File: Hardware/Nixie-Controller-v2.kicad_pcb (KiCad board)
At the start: 4 copper layers, 220 x 65 mm, 216 parts, among them J7 12V DC JACK, U1 MAX1771, U10 74HC4067, U11 M41T01, U12 STM32F103C8, U13 OPA180, U14 74HC4067, U15 OPA180, U16 74HC4067, U17 OPA180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

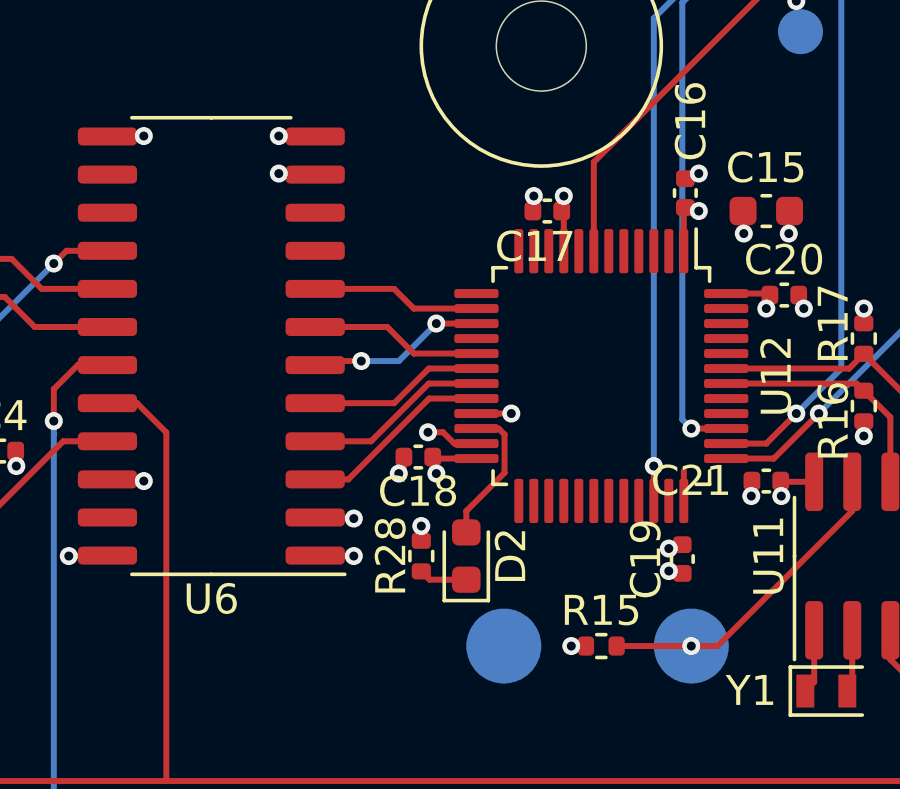
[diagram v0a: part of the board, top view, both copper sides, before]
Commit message: Connect shift register to SPI ports
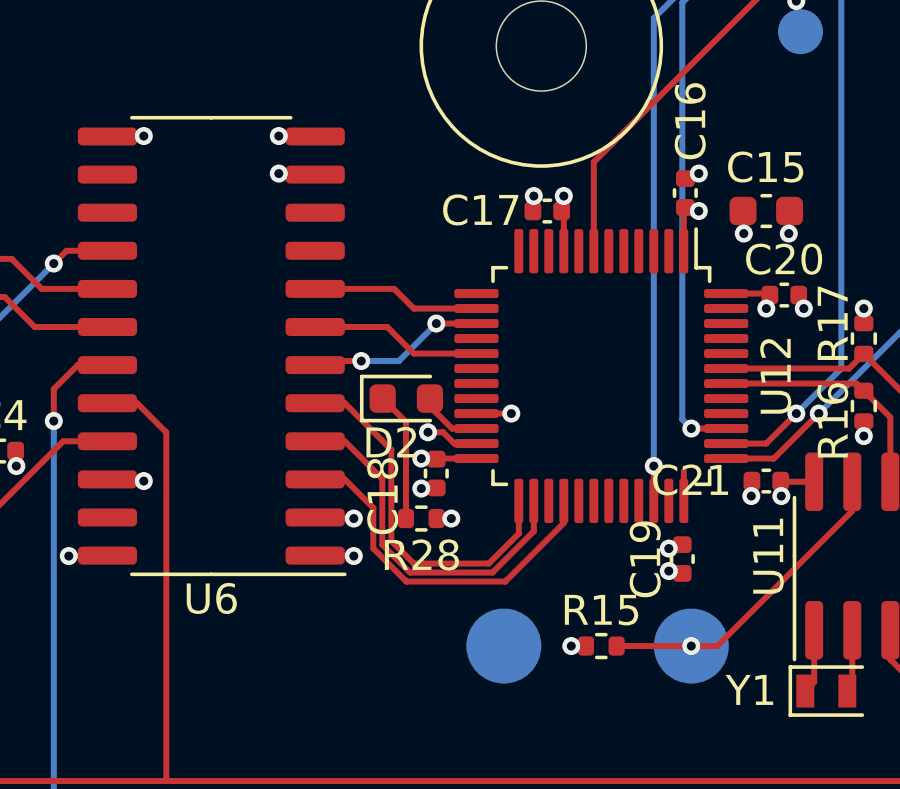
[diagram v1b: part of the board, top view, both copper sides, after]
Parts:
- moved D2 5.62 mm to (119.5, 74.8), turned to 0 degrees
- moved R28 1.25 mm to (120.0, 78.8), turned to 180 degrees
- moved C18 0.81 mm to (120.5, 77.2), turned to 270 degrees
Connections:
- U12 pad 18: 3V3_SR_LATCH -> Net-(U12-Pad18)
- U12 pad 19: 3V3_SR_SHIFT -> Net-(U12-Pad19)
- U12 pad 20: 3V3_SR_DATA -> Net-(U12-Pad20)
- U12 pad 25: Net-(U12-Pad25) -> 3V3_SR_nCS
- U12 pad 26: Net-(U12-Pad26) -> 3V3_SR_SCK
- U12 pad 28: Net-(U12-Pad28) -> 3V3_SR_MOSI
- U6 pad 3: 3V3_SR_DATA -> 3V3_SR_MOSI
- U6 pad 4: 3V3_SR_SHIFT -> 3V3_SR_SCK
- U6 pad 5: 3V3_SR_LATCH -> 3V3_SR_nCS
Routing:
- net 3V3_SR_nCS: track 0.00 -> 12.3 mm
- net 3V3_SR_MOSI: track 0.00 -> 12.0 mm
- net 3V3_SR_SCK: track 0.00 -> 12.0 mm
- net 3V3_SR_DATA: track 6.49 -> 0.00 mm
- net 3V3_SR_SHIFT: track 6.17 -> 0.00 mm
- net 3V3_SR_LATCH: track 5.85 -> 0.00 mm
- net Net-(D2-Pad1): track 1.61 -> 4.32 mm
- net Net-(D2-Pad2): track 4.81 -> 2.12 mm

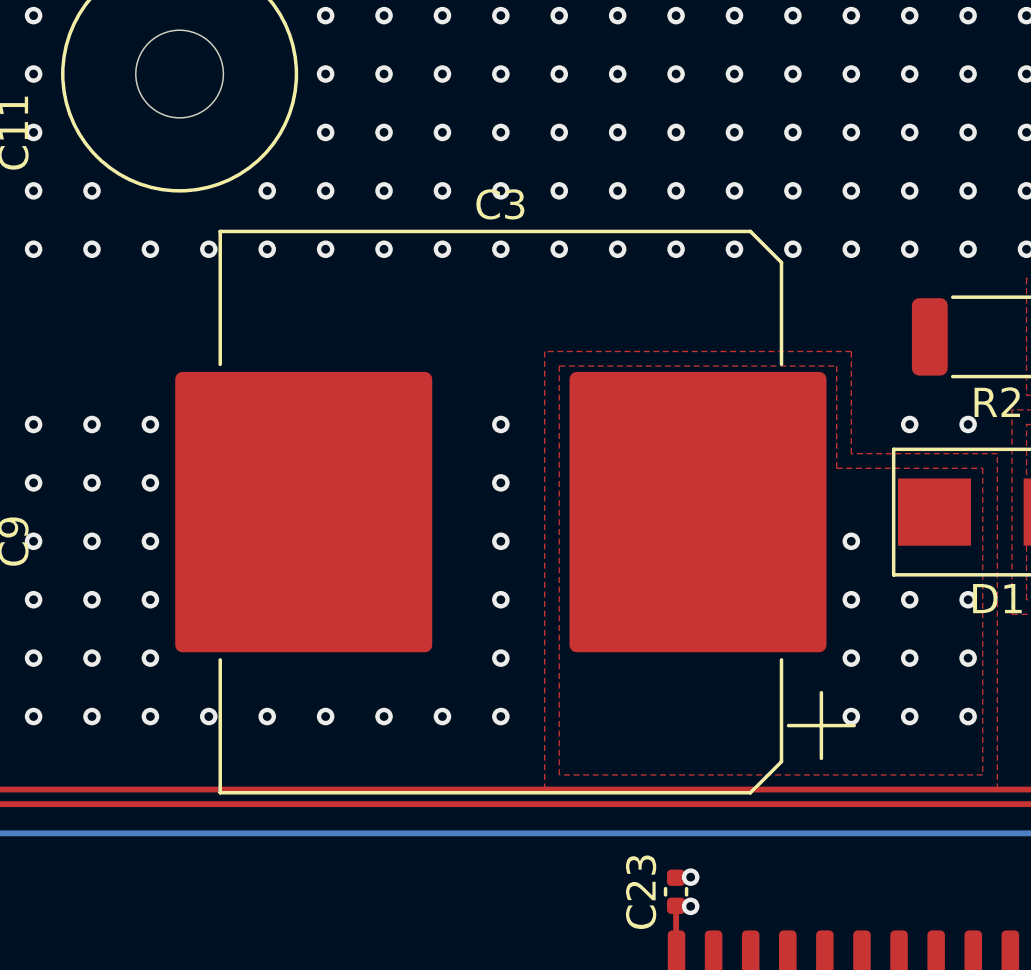
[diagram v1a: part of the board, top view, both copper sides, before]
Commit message: Switch HV output cap to 10uF
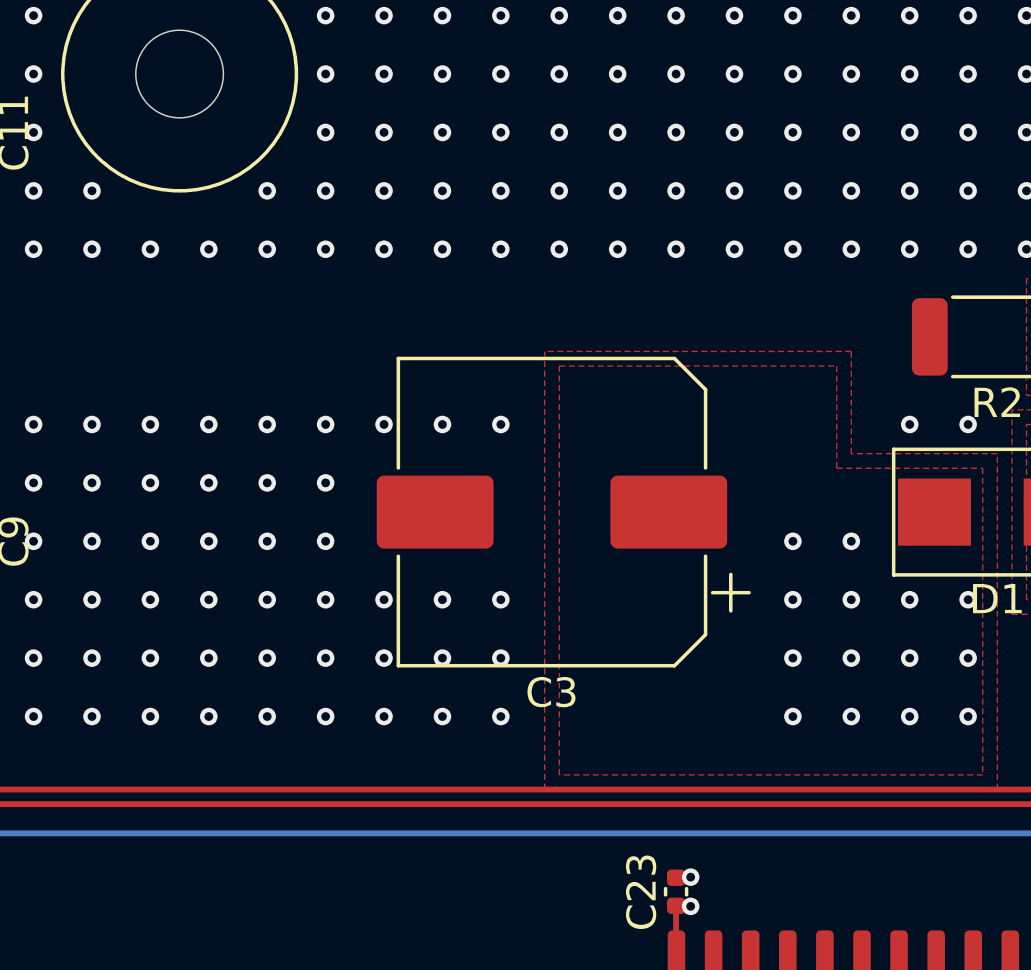
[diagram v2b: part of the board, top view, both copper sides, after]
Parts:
- C3: value 22uF -> 10uF; footprint Capacitor_SMD:CP_Elec_18x17.5 -> Capacitor_SMD:CP_Elec_10x10
- moved C3 1.75 mm to (206.8, 78.0)
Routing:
- net GND: vias 413 -> 432
- net +HV: vias 11 -> 15

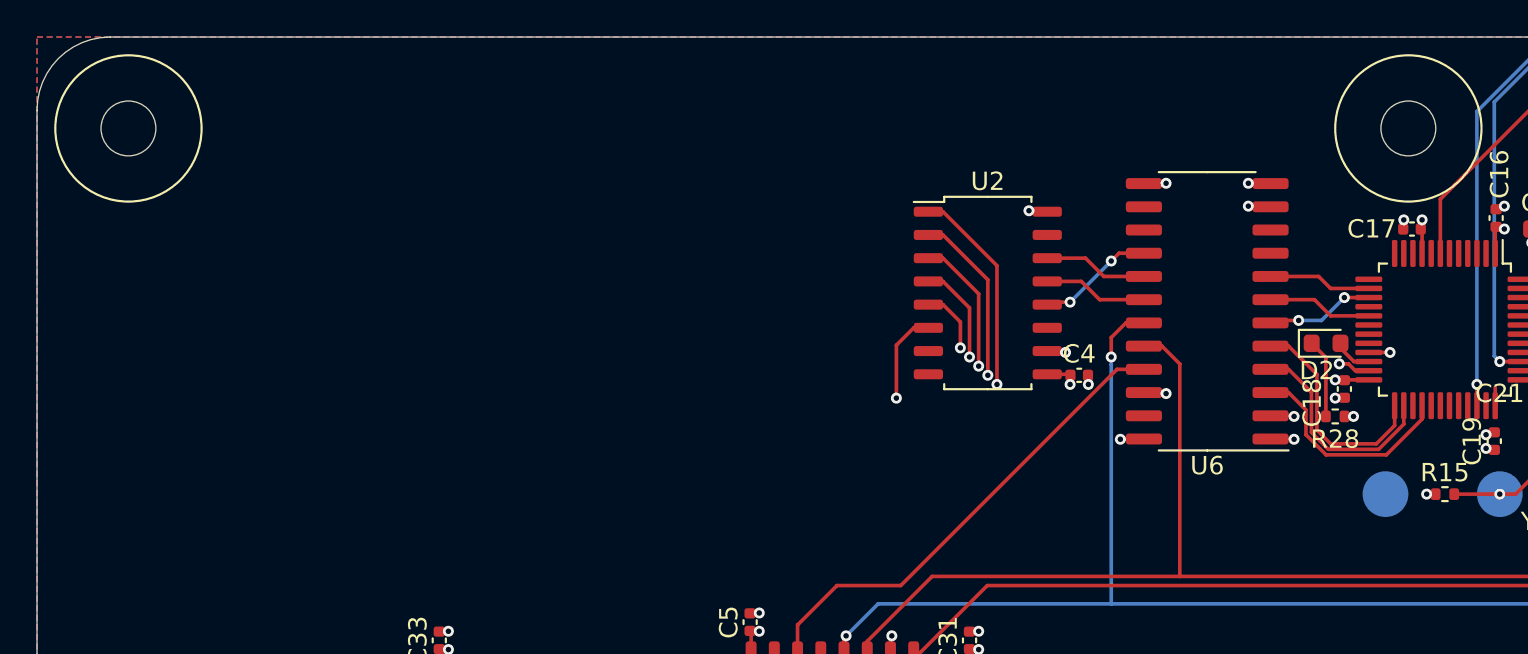
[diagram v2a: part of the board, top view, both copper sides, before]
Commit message: Add ESP WiFi module
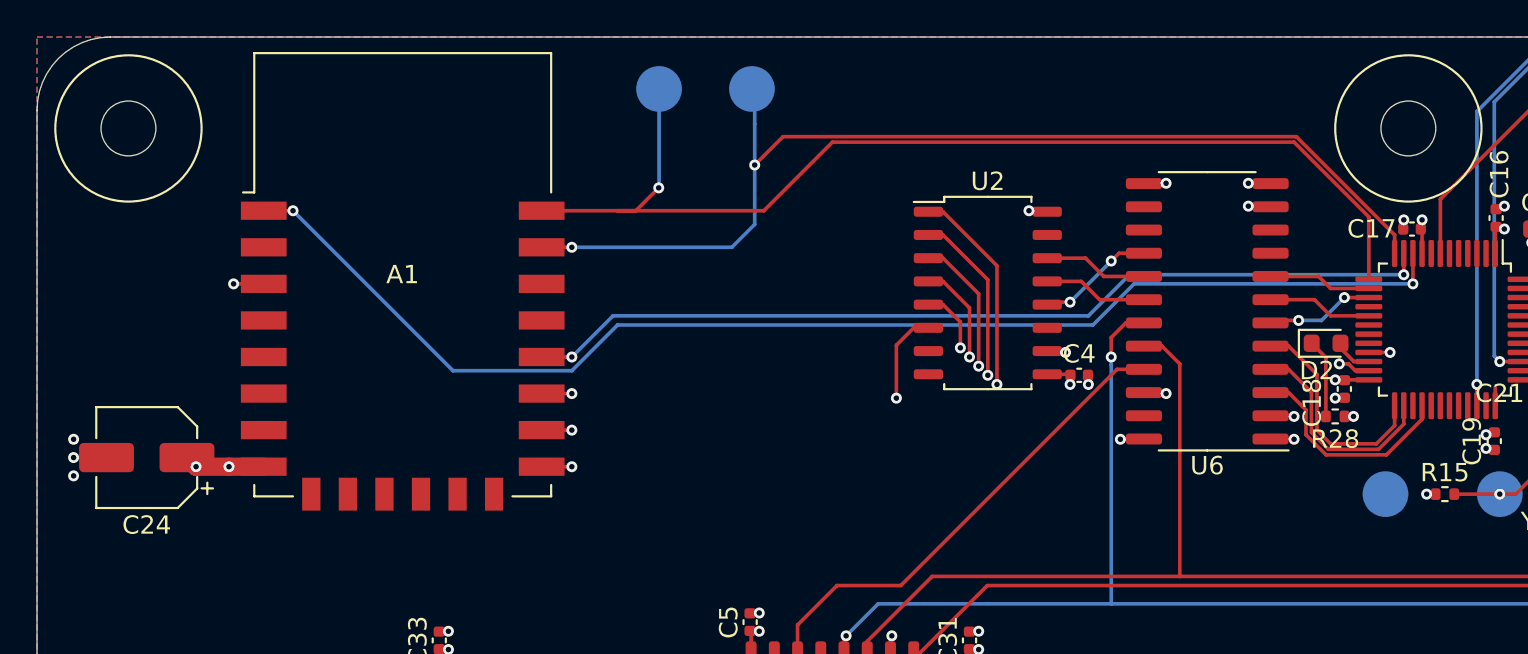
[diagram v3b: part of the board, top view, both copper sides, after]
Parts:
- added A1: ESP-12F, RF_Module:ESP-12E, F.Cu at (69.0, 71.0)
- added C24: 47uF, Capacitor_SMD:CP_Elec_5x5.3, F.Cu at (55.0, 81.0)
- added TP17: TX, TestPoint:TestPoint_Pad_D2.5mm, B.Cu at (83.0, 60.8)
- added TP18: RX, TestPoint:TestPoint_Pad_D2.5mm, B.Cu at (88.1, 60.8)
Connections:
- U12 pad 10: Net-(U12-Pad10) -> ESP_nRST
- U12 pad 11: Net-(U12-Pad11) -> ESP_RUN
- U12 pad 12: Net-(U12-Pad12) -> ESP_TX
- U12 pad 13: Net-(U12-Pad13) -> ESP_RX
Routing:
- net ESP_nRST: track 0.00 -> 70.1 mm, vias 0 -> 2
- net ESP_RX: track 0.00 -> 60.1 mm, vias 0 -> 1
- net ESP_TX: track 0.00 -> 58.5 mm, vias 0 -> 2
- net ESP_RUN: track 0.00 -> 50.2 mm, vias 0 -> 2
- net +3V3: track 23.7 -> 31.4 mm, vias 29 -> 33
- net GND: track 68.8 -> 72.1 mm, vias 432 -> 437
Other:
- board text added: "RX"
- board text added: "TX"

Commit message: Add author and HV info to silkscreen
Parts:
- added REF**: Symbol_Highvoltage_Type1_CopperTop_Small, Symbol:Symbol_Highvoltage_Type1_CopperTop_Small, B.Cu at (87.0, 114.0)
- added REF**: Symbol_Highvoltage_Type1_CopperTop_Small, Symbol:Symbol_Highvoltage_Type1_CopperTop_Small, B.Cu at (116.0, 114.0)
- added REF**: Symbol_Highvoltage_Type1_CopperTop_Small, Symbol:Symbol_Highvoltage_Type1_CopperTop_Small, B.Cu at (157.0, 114.0)
- added REF**: Symbol_Highvoltage_Type1_CopperTop_Small, Symbol:Symbol_Highvoltage_Type1_CopperTop_Small, B.Cu at (186.0, 114.0)
- added REF**: Symbol_Highvoltage_Type1_CopperTop_Small, Symbol:Symbol_Highvoltage_Type1_CopperTop_Small, B.Cu at (227.0, 114.0)
- added REF**: Symbol_Highvoltage_Type1_CopperTop_Small, Symbol:Symbol_Highvoltage_Type1_CopperTop_Small, B.Cu at (256.0, 114.0)
- added REF**: Symbol_Highvoltage_Type1_CopperTop_Small, Symbol:Symbol_Highvoltage_Type1_CopperTop_Small, F.Cu at (215.0, 75.0)
- added REF**: OSHW-Logo2_7.3x6mm_SilkScreen, Symbol:OSHW-Logo2_7.3x6mm_SilkScreen, F.Cu at (110.0, 61.0)
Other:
- board text added: "DANGER HIGH VOLTAGE"
- board text added: "Second Generation Nixie Controller"
- board text added: "github.com/DanielHeEGG/Nixie-Controller-v2"

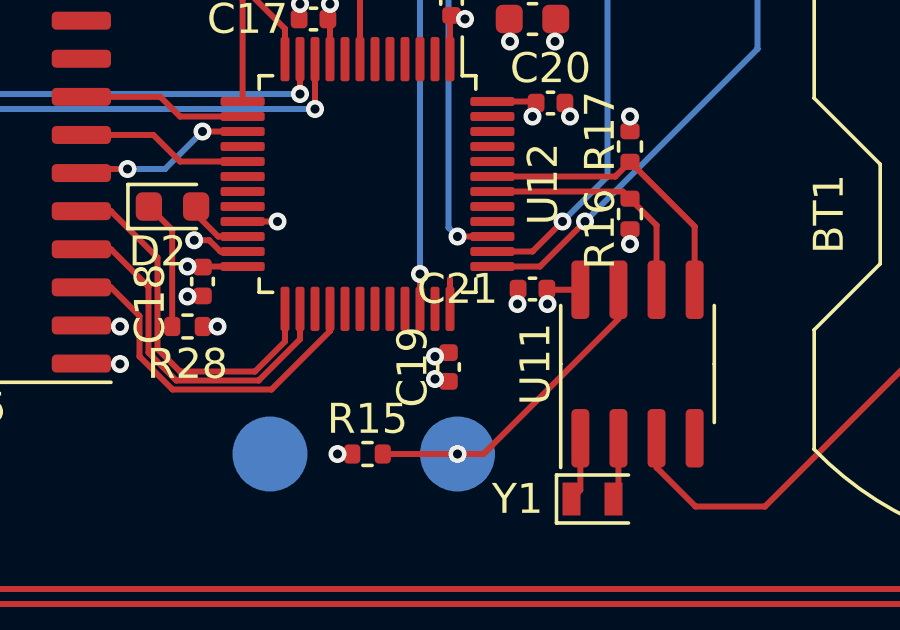
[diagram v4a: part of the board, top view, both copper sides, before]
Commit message: Fix unconnected bypass cap
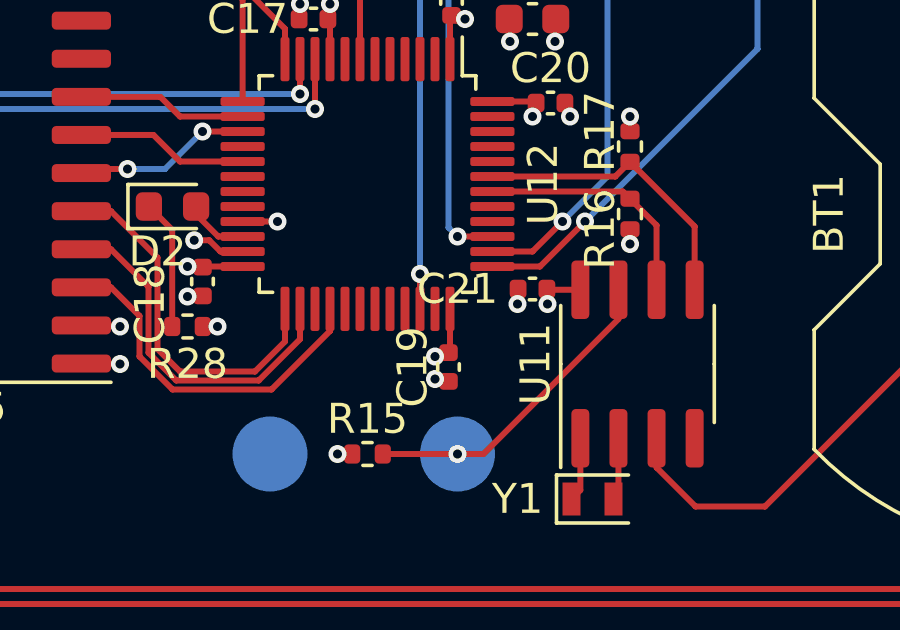
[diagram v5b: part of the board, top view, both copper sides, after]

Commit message: Add revision info to silkscreen
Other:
- board text added: "Revision: v2.0-pre2"
